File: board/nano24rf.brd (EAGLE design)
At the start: 17.8 x 50 mm, 20 parts

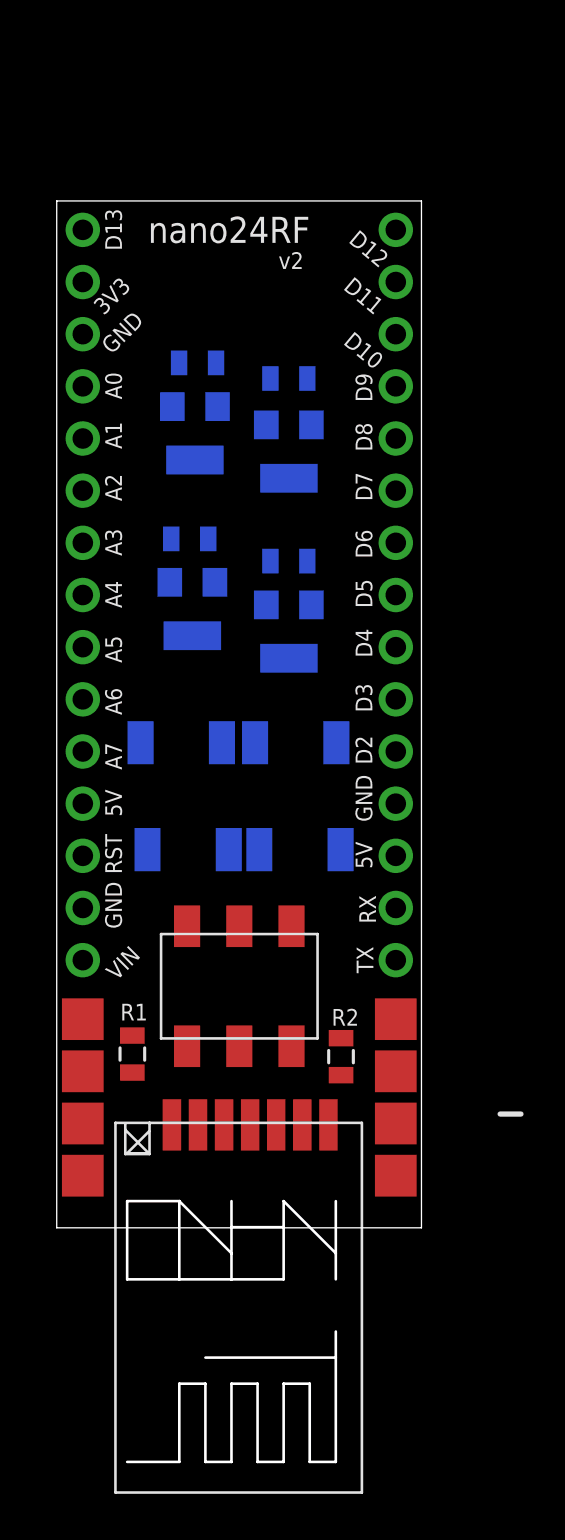
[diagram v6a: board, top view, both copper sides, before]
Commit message: fixed bad packges for 2x3 and smdx07
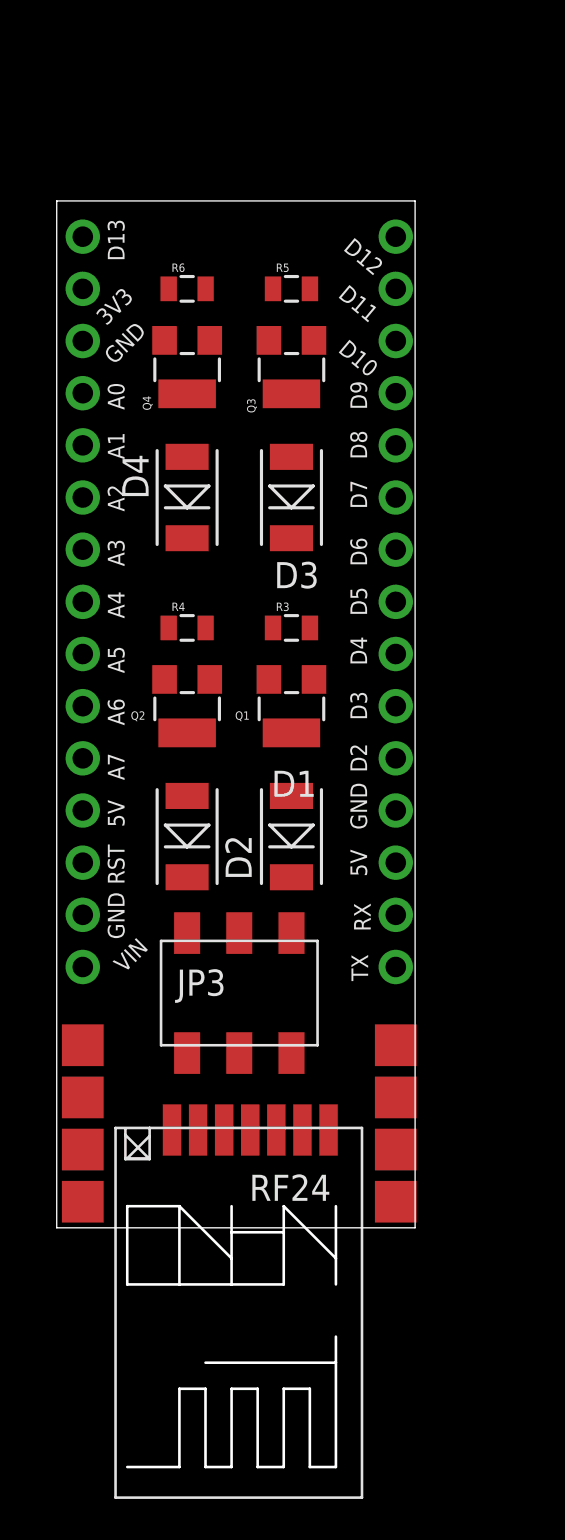
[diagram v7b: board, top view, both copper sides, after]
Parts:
- removed R1, R2: (no value), ATTAMI-V0.00:0805
- removed U$6, U$8: FATPAD4, nano24rf:FATPAD4
- removed U$7: 1X7-SMDPADS, nano24rf:SMD1,27-2,54
- added MOSFET-12, MOSFET-34: FATPAD4, nano24rf:FATPAD4
- added RF24: 1X7-SMDPADS, nano24rf:SMD1,27-2,54
- moved D3 13.1 mm to (11.4, 35.6), flipped to the top, turned to 90 degrees
- moved D4 13.1 mm to (6.35, 35.6), flipped to the top, turned to 90 degrees
- moved Q1 6.76 mm to (11.4, 25.4), flipped to the top
- moved R6 6.60 mm to (6.35, 45.7), flipped to the top
- moved R3 6.58 mm to (11.4, 29.2), flipped to the top
- moved Q4 6.44 mm to (6.35, 41.9), flipped to the top
- moved Q2 6.14 mm to (6.35, 25.4), flipped to the top
- moved R4 5.93 mm to (6.35, 29.2), flipped to the top
- moved R5 5.82 mm to (11.4, 45.7), flipped to the top
- moved Q3 5.70 mm to (11.4, 41.9), flipped to the top
- moved D1 0.76 mm to (11.4, 19.1), flipped to the top, turned to 90 degrees
- moved D2 0.64 mm to (6.35, 19.1), flipped to the top, turned to 90 degrees
- moved JP3 0.33 mm to (8.89, 11.4)
- moved JP1 0.33 mm to (1.27, 30.5)
- moved JP2 0.33 mm to (16.5, 30.5)
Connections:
- removed net D3: JP2.10
- removed net N$6: R1.2, R2.2, U$7.1
- removed net S$1: U$6.P$4, U$7.4
- net 3V3: now also RF24.7
- net 5V: no longer R1.1
- net CE: now also RF24.5; no longer U$7.2
- net CSN: now also RF24.4; no longer U$7.3
- net FET01: now also MOSFET-12.P$1; no longer U$8.P$1
- net FET02: now also MOSFET-12.P$3; no longer U$8.P$3
- net FET03: now also MOSFET-34.P$1; no longer U$6.P$1
- net FET04: now also MOSFET-34.P$3; no longer U$6.P$3
- net GND: now also MOSFET-12.P$4, MOSFET-34.P$4, RF24.6; no longer R2.1, U$8.P$4
- net MISO: now also RF24.1; no longer U$7.5
- net MOSI: now also RF24.2; no longer U$7.6
- net SCK: now also RF24.3; no longer U$7.7
- net VIN: now also MOSFET-12.P$2, MOSFET-34.P$2; no longer U$6.P$2, U$8.P$2
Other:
- board size 17.8 x 50 mm -> 17.4 x 50 mm
- board text removed: "nano24RF"
- board text removed: "v2"

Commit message: routed ver3, no canstlation
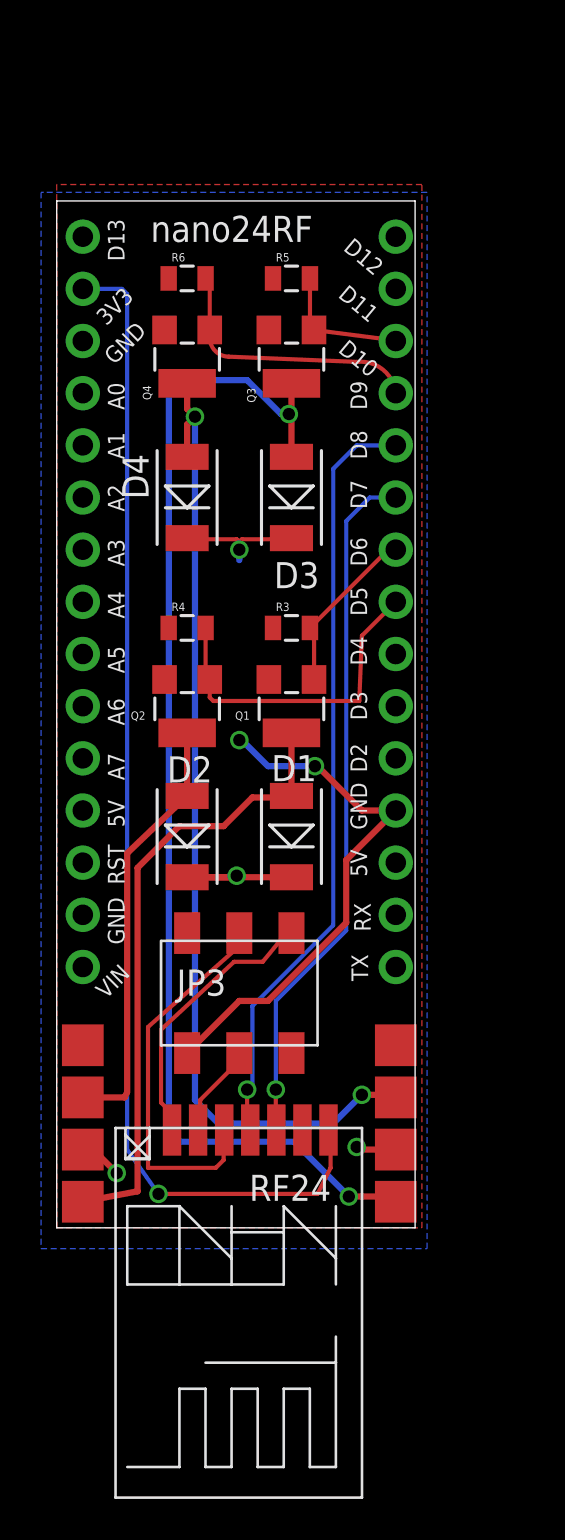
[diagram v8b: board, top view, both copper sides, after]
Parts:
- moved Q3 0.51 mm to (11.4, 42.4)
- moved Q4 0.51 mm to (6.35, 42.4)
- moved R5 0.51 mm to (11.4, 46.2)
- moved R6 0.51 mm to (6.35, 46.2)
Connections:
- net SCK renamed CSK
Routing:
- net FET03: track 0.00 -> 59.7 mm, vias 0 -> 2
- net 3V3: track 0.00 -> 57.6 mm, vias 0 -> 1
- net FET04: track 0.00 -> 48.1 mm, vias 0 -> 2
- net CSN: track 0.00 -> 37.5 mm, vias 0 -> 1
- net CE: track 0.00 -> 34.0 mm, vias 0 -> 1
- net FET01: track 0.00 -> 30.5 mm
- net GND: track 0.00 -> 26.3 mm, vias 0 -> 2
- net FET02: track 0.00 -> 21.1 mm
- net CSK: track 0.00 -> 18.7 mm
- net VIN: track 0.00 -> 18.4 mm, vias 0 -> 4
- net D5: track 0.00 -> 16.3 mm
- net MISO: track 0.00 -> 13.4 mm
- net D9: track 0.00 -> 12.9 mm
- net D6: track 0.00 -> 8.35 mm
- net D10: track 0.00 -> 6.62 mm
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- added copper zone on layer 1, net GND
- added copper zone on layer 16, net VIN
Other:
- board text added: "nano24RF"
